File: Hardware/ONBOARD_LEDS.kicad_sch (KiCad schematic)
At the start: 38 parts, among them U10 SN74HC594DR, U9 SN74HC594DR

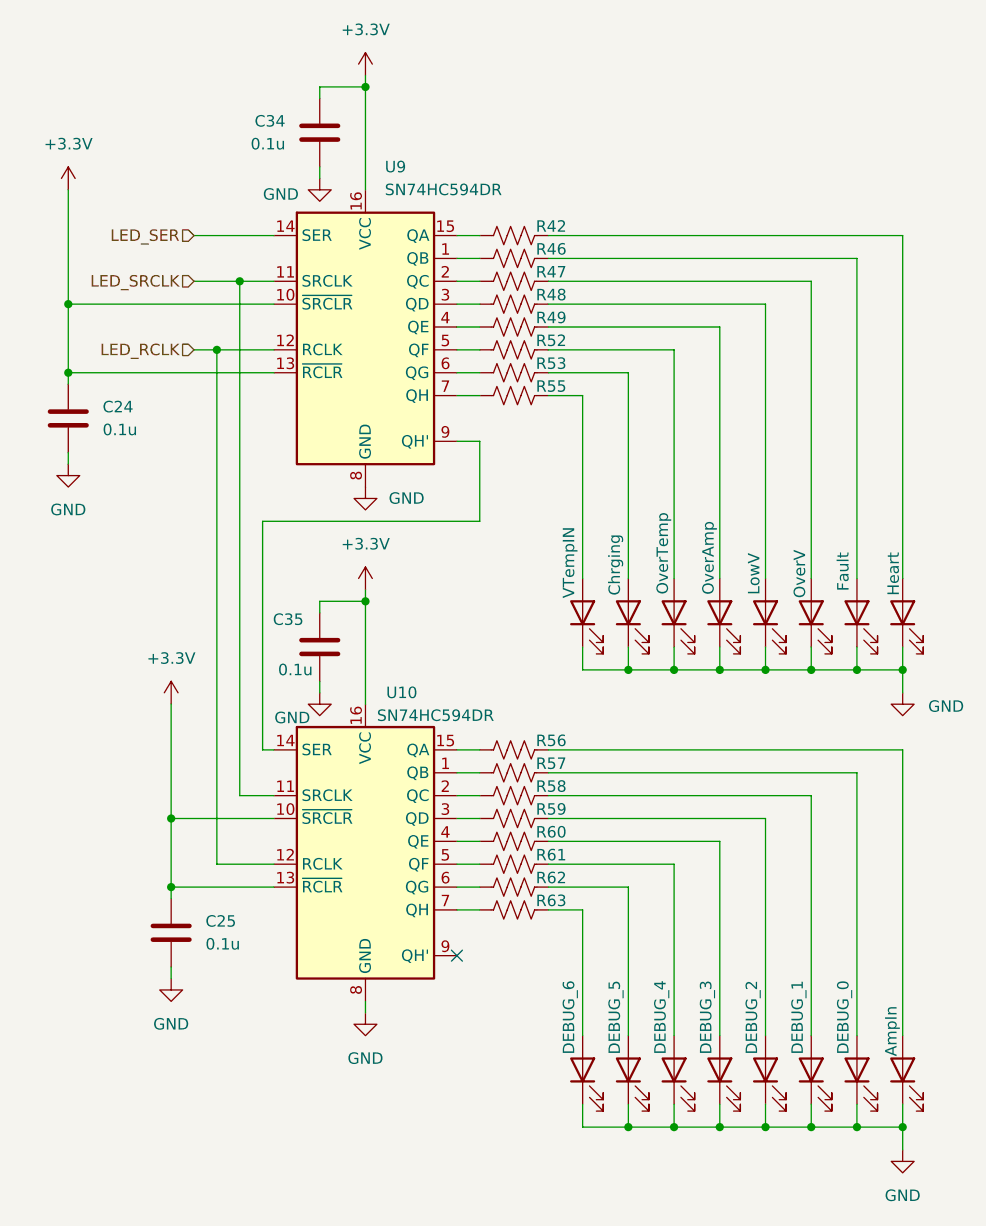
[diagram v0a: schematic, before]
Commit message: Schematic polishes, layout WIP
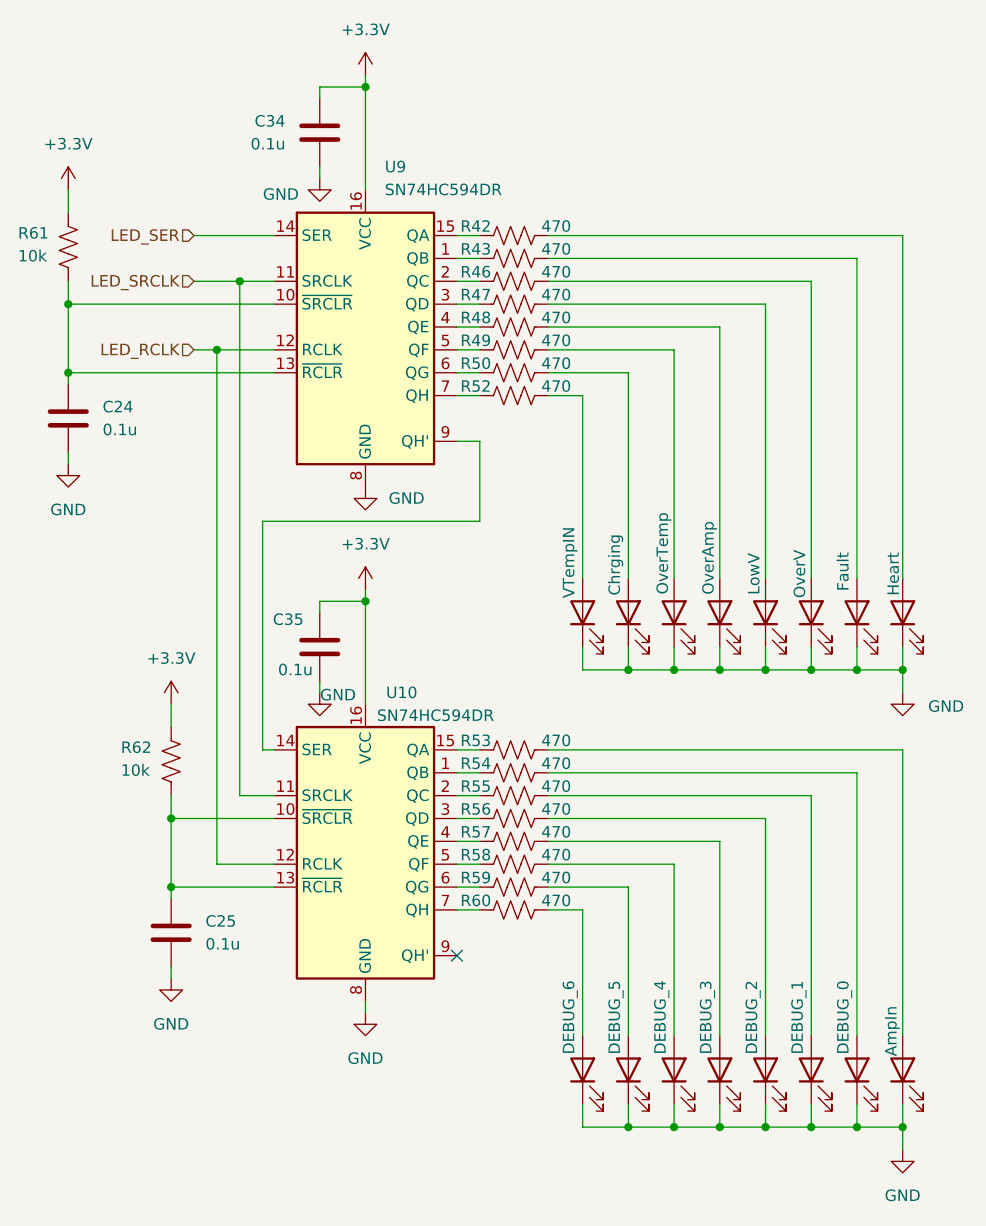
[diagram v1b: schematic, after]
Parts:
- removed R63: 150, Resistor_SMD:R_0603_1608Metric, symbol Device:R_US
- added R43, R50, R54: 470, Resistor_SMD:R_0603_1608Metric, symbol Device:R_US
- C24, C25, C34, C35: footprint Capacitor_SMD:C_0603_1608Metric_Pad1.08x0.95mm_HandSolder -> Capacitor_SMD:C_0603_1608Metric
- R42, R46, R47, R48, R49, R52, R53, R55, R57, R58, R59, R60: value 150 -> 470; P/N CRCW0603150RFKEC -> CRCW1206470RFKEA
- R56: value 120 -> 470; P/N CRCW0603120RFKEC -> CRCW1206470RFKEA
- R61, R62: value 150 -> 10k; Manufactuerer Vishay -> (none); Mouser Part Number (none) -> 71-CRCW060310K0FKEI; P/N CRCW0603150RFKEC -> CRCW060310K0FKEI
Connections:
- net +3.3V: now also R61.1, R62.1; no longer C24.1, C25.1, U10.10 (~{SRCLR}), U10.13 (~{RCLR}), U9.10 (~{SRCLR}), U9.13 (~{RCLR})
- net at OverTemp1.2 (A): now also R49.2; no longer R52.2
- net at U9.6 (QG): now also R50.1; no longer R53.1
- net at Chrging1.2 (A): now also R50.2; no longer R53.2
- net at DEBUG_3.2 (A): now also R57.2; no longer R60.2
- net at R47.1: now also U9.3 (QD); no longer U9.2 (QC)
- net at R47.2: now also LowV1.2 (A); no longer OverV1.2 (A)
- net at R61.2: now also C24.1, U9.10 (~{SRCLR}), U9.13 (~{RCLR}); no longer DEBUG_4.2 (A)
- net at U10.6 (QG): now also R59.1; no longer R62.1
- net at DEBUG_5.2 (A): now also R59.2; no longer R62.2
- net at R48.2: now also OverAmp1.2 (A); no longer LowV1.2 (A)
- net at DEBUG_6.2 (A): now also R60.2
- net at U10.4 (QE): now also R57.1; no longer R60.1
- net at U10.2 (QC): now also R55.1; no longer R58.1
- net at R58.2: now also DEBUG_4.2 (A); no longer DEBUG_1.2 (A)
- net at U9.4 (QE): now also R48.1; no longer R49.1
- net at VTempIN1.2 (A): now also R52.2; no longer R55.2
- net at R56.1: now also U10.3 (QD); no longer U10.15 (QA)
- net at R56.2: now also DEBUG_2.2 (A); no longer AmpIn1.2 (A)
- net at DEBUG_0.2 (A): now also R54.2; no longer R57.2
- net at R46.1: now also U9.2 (QC); no longer U9.1 (QB)
- net at R52.1: now also U9.7 (QH); no longer U9.5 (QF)
- net at R46.2: now also OverV1.2 (A); no longer Fault1.2 (A)
- net at U10.1 (QB): now also R54.1; no longer R57.1
- net at U10.5 (QF): now also R58.1; no longer R61.1
- net at U10.7 (QH): now also R60.1
- new net: R43.1, U9.1 (QB)
- new net: Fault1.2 (A), R43.2
- new net: C25.1, R62.2, U10.10 (~{SRCLR}), U10.13 (~{RCLR})
- new net: R53.1, U10.15 (QA)
- new net: AmpIn1.2 (A), R53.2
- new net: DEBUG_1.2 (A), R55.2
- new net: R49.1, U9.5 (QF)

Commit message: RevB layout completed
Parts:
- D14: renamed from Heart1; value Heart -> DEBUG
- D15: renamed from Fault1; value Fault -> ModuleFault[0]
- D16: renamed from OverV1; value OverV -> ModuleFault[1]
- D17: renamed from LowV1; value LowV -> ModuleFault[2]
- D18: renamed from OverAmp1; value OverAmp -> ModuleFault[3]
- D19: renamed from OverTemp1; value OverTemp -> ModuleFault[4]
- D20: renamed from Chrging1; value Chrging -> WatchdogErr
- D21: renamed from VTempIN1; value VTempIN -> AmpIN
- D22: renamed from AmpIn1; value AmpIn -> VTempIN
- D23: renamed from DEBUG_0; value DEBUG_0 -> Chrging
- D24: renamed from DEBUG_1; value DEBUG_1 -> OverTemp
- D25: renamed from DEBUG_2; value DEBUG_2 -> OverAmp
- D26: renamed from DEBUG_3; value DEBUG_3 -> LowV
- D28: renamed from DEBUG_5; value DEBUG_5 -> Fault
- D29: renamed from DEBUG_6; value DEBUG_6 -> Heart
- D30: renamed from DEBUG_4; value DEBUG_4 -> OverV
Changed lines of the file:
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@@
 		(on_board yes)
 		(dnp no)
-		(property "Reference" "OverTemp1"
+		(property "Reference" "D19"
 			(at 191.77 94.2975 0)
 			(effects
@@
 			)
 		)
-		(property "Value" "OverTemp"
-			(at 182.88 86.106 0)
+		(property "Value" "ModuleFault[4]"
+			(at 182.372 83.312 0)
 			(effects
 				(font
@@
 			(project "BPS-Leader"
 				(path "/fb37da34-e420-4994-8cc1-079e8c0fa48e/ec328d6f-4db5-4eba-b704-0212808a8e56"
-					(reference "OverTemp1")
+					(reference "D19")
 					(unit 1)
 				)
@@
 		(on_board yes)
 		(dnp no)
-		(property "Reference" "DEBUG_3"
+		(property "Reference" "D26"
 			(at 196.85 145.0975 0)
 			(effects
@@
 			)
 		)
-		(property "Value" "DEBUG_3"
+		(property "Value" "LowV"
 			(at 187.706 137.668 0)
 			(effects
@@
 			(project "BPS-Leader"
 				(path "/fb37da34-e420-4994-8cc1-079e8c0fa48e/ec328d6f-4db5-4eba-b704-0212808a8e56"
-					(reference "DEBUG_3")
+					(reference "D26")
 					(unit 1)
 				)
@@
 		(on_board yes)
 		(dnp no)
-		(property "Reference" "DEBUG_4"
+		(property "Reference" "D30"
 			(at 191.77 145.0975 0)
 			(effects
@@
 			)
 		)
-		(property "Value" "DEBUG_4"
+		(property "Value" "OverV"
 			(at 182.626 137.668 0)
 			(effects
@@
 			(project "BPS-Leader"
 				(path "/fb37da34-e420-4994-8cc1-079e8c0fa48e/ec328d6f-4db5-4eba-b704-0212808a8e56"
-					(reference "DEBUG_4")
+					(reference "D30")
 					(unit 1)
 				)
@@
 		(on_board yes)
 		(dnp no)
-		(property "Reference" "Heart1"
+		(property "Reference" "D14"
 			(at 217.17 94.2975 0)
 			(effects
@@
 			)
 		)
-		(property "Value" "Heart"
-			(at 208.534 88.392 0)
+		(property "Value" "DEBUG"
+			(at 208.026 87.122 0)
 			(effects
 				(font
@@
 			(project "BPS-Leader"
 				(path "/fb37da34-e420-4994-8cc1-079e8c0fa48e/ec328d6f-4db5-4eba-b704-0212808a8e56"
-					(reference "Heart1")
+					(reference "D14")
 					(unit 1)
 				)
@@
 		(on_board yes)
 		(dnp no)
-		(property "Reference" "LowV1"
+		(property "Reference" "D17"
 			(at 201.93 94.2975 0)
 			(effects
@@
 			)
 		)
-		(property "Value" "LowV"
-			(at 193.04 88.392 0)
+		(property "Value" "ModuleFault[2]"
+			(at 193.04 83.566 0)
 			(effects
 				(font
@@
 			(project "BPS-Leader"
 				(path "/fb37da34-e420-4994-8cc1-079e8c0fa48e/ec328d6f-4db5-4eba-b704-0212808a8e56"
-					(reference "LowV1")
+					(reference "D17")
 					(unit 1)
 				)
@@
 		(on_board yes)
 		(dnp no)
-		(property "Reference" "DEBUG_6"
+		(property "Reference" "D29"
 			(at 181.61 145.0975 0)
 			(effects
@@
 			)
 		)
-		(property "Value" "DEBUG_6"
+		(property "Value" "Heart"
 			(at 172.466 137.668 0)
 			(effects
@@
 			(project "BPS-Leader"
 				(path "/fb37da34-e420-4994-8cc1-079e8c0fa48e/ec328d6f-4db5-4eba-b704-0212808a8e56"
-					(reference "DEBUG_6")
+					(reference "D29")
 					(unit 1)
 				)
@@
 		(on_board yes)
 		(dnp no)
-		(property "Reference" "Chrging1"
+		(property "Reference" "D20"
 			(at 186.69 94.2975 0)
 			(effects
@@
 			)
 		)
-		(property "Value" "Chrging"
-			(at 177.546 87.376 0)
+		(property "Value" "WatchdogErr"
+			(at 177.292 84.328 0)
 			(effects
 				(font
@@
 			(project "BPS-Leader"
 				(path "/fb37da34-e420-4994-8cc1-079e8c0fa48e/ec328d6f-4db5-4eba-b704-0212808a8e56"
-					(reference "Chrging1")
+					(reference "D20")
 					(unit 1)
 				)
@@
 		(on_board yes)
 		(dnp no)
-		(property "Reference" "DEBUG_5"
+		(property "Reference" "D28"
 			(at 186.69 145.0975 0)
 			(effects
@@
 			)
 		)
-		(property "Value" "DEBUG_5"
+		(property "Value" "Fault"
 			(at 177.546 137.668 0)
 			(effects
@@
 			(project "BPS-Leader"
 				(path "/fb37da34-e420-4994-8cc1-079e8c0fa48e/ec328d6f-4db5-4eba-b704-0212808a8e56"
-					(reference "DEBUG_5")
+					(reference "D28")
 					(unit 1)
 				)
@@
 		(on_board yes)
 		(dnp no)
-		(property "Reference" "VTempIN1"
+		(property "Reference" "D21"
 			(at 181.61 94.2975 0)
 			(effects
@@
 			)
 		)
-		(property "Value" "VTempIN"
+		(property "Value" "AmpIN"
 			(at 172.466 87.122 0)
 			(effects
@@
 			(project "BPS-Leader"
 				(path "/fb37da34-e420-4994-8cc1-079e8c0fa48e/ec328d6f-4db5-4eba-b704-0212808a8e56"
-					(reference "VTempIN1")
+					(reference "D21")
 					(unit 1)
 				)
@@
 		(on_board yes)
 		(dnp no)
-		(property "Reference" "DEBUG_1"
+		(property "Reference" "D24"
 			(at 207.01 145.0975 0)
 			(effects
@@
 			)
 		)
-		(property "Value" "DEBUG_1"
+		(property "Value" "OverTemp"
 			(at 197.866 137.668 0)
 			(effects
@@
 			(project "BPS-Leader"
 				(path "/fb37da34-e420-4994-8cc1-079e8c0fa48e/ec328d6f-4db5-4eba-b704-0212808a8e56"
-					(reference "DEBUG_1")
+					(reference "D24")
 					(unit 1)
 				)
@@
 		(on_board yes)
 		(dnp no)
-		(property "Reference" "DEBUG_0"
+		(property "Reference" "D23"
 			(at 212.09 145.0975 0)
 			(effects
@@
 			)
 		)
-		(property "Value" "DEBUG_0"
+		(property "Value" "Chrging"
 			(at 202.946 137.668 0)
 			(effects
@@
 			(project "BPS-Leader"
 				(path "/fb37da34-e420-4994-8cc1-079e8c0fa48e/ec328d6f-4db5-4eba-b704-0212808a8e56"
-					(reference "DEBUG_0")
+					(reference "D23")
 					(unit 1)
 				)
@@
 		(on_board yes)
 		(dnp no)
-		(property "Reference" "DEBUG_2"
+		(property "Reference" "D25"
 			(at 201.93 145.0975 0)
 			(effects
@@
 			)
 		)
-		(property "Value" "DEBUG_2"
+		(property "Value" "OverAmp"
 			(at 192.786 137.668 0)
 			(effects
@@
 			(project "BPS-Leader"
 				(path "/fb37da34-e420-4994-8cc1-079e8c0fa48e/ec328d6f-4db5-4eba-b704-0212808a8e56"
-					(reference "DEBUG_2")
+					(reference "D25")
 					(unit 1)
 				)
@@
 		(on_board yes)
 		(dnp no)
-		(property "Reference" "OverAmp1"
+		(property "Reference" "D18"
 			(at 196.85 94.2975 0)
 			(effects
@@
 			)
 		)
-		(property "Value" "OverAmp"
-			(at 187.96 86.614 0)
+		(property "Value" "ModuleFault[3]"
+			(at 187.706 83.566 0)
 			(effects
 				(font
@@
 			(project "BPS-Leader"
 				(path "/fb37da34-e420-4994-8cc1-079e8c0fa48e/ec328d6f-4db5-4eba-b704-0212808a8e56"
-					(reference "OverAmp1")
+					(reference "D18")
 					(unit 1)
 				)
@@
 		(on_board yes)
 		(dnp no)
-		(property "Reference" "AmpIn1"
+		(property "Reference" "D22"
 			(at 217.17 145.0975 0)
 			(effects
@@
 			)
 		)
-		(property "Value" "AmpIn"
+		(property "Value" "VTempIN"
 			(at 208.28 139.192 0)
 			(effects
@@
 			(project "BPS-Leader"
 				(path "/fb37da34-e420-4994-8cc1-079e8c0fa48e/ec328d6f-4db5-4eba-b704-0212808a8e56"
-					(reference "AmpIn1")
+					(reference "D22")
 					(unit 1)
 				)
@@
 		(on_board yes)
 		(dnp no)
-		(property "Reference" "Fault1"
+		(property "Reference" "D15"
 			(at 212.09 94.2975 0)
 			(effects
@@
 			)
 		)
-		(property "Value" "Fault"
-			(at 202.946 88.138 0)
+		(property "Value" "ModuleFault[0]"
+			(at 202.692 83.312 0)
 			(effects
 				(font
@@
 			(project "BPS-Leader"
 				(path "/fb37da34-e420-4994-8cc1-079e8c0fa48e/ec328d6f-4db5-4eba-b704-0212808a8e56"
-					(reference "Fault1")
+					(reference "D15")
 					(unit 1)
 				)
@@
 		(on_board yes)
 		(dnp no)
-		(property "Reference" "OverV1"
+		(property "Reference" "D16"
 			(at 207.01 94.2975 0)
 			(effects
@@
 			)
 		)
-		(property "Value" "OverV"
-			(at 198.12 88.392 0)
+		(property "Value" "ModuleFault[1]"
+			(at 197.612 83.566 0)
 			(effects
 				(font
@@
 			(project "BPS-Leader"
 				(path "/fb37da34-e420-4994-8cc1-079e8c0fa48e/ec328d6f-4db5-4eba-b704-0212808a8e56"
-					(reference "OverV1")
+					(reference "D16")
 					(unit 1)
 				)

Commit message: JLC Production Files
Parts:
- C24, C25, C34, C35: LCSC (none) -> C14663
- D14, D20, D21, D22, D23, D24, D25, D26, D28, D29, D30: LCSC (none) -> C84263
- D15, D16, D17, D18, D19: LCSC (none) -> C7371904
- R42, R43, R46, R47, R48, R49, R50, R52, R53, R54, R55, R56, R57, R58, R59, R60: LCSC (none) -> C23179
- R61, R62: LCSC (none) -> C25804
- U10, U9: LCSC (none) -> C91727

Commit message: condensed custom lirbraries
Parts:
- U10, U9: footprint SN74HC594DR:SOIC127P600X175-16N -> CustomKiCad-Library:SOIC127P600X175-16N
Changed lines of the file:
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@@
 			)
 		)
-		(property "Footprint" "SN74HC594DR:SOIC127P600X175-16N"
+		(property "Footprint" "CustomKiCad-Library:SOIC127P600X175-16N"
 			(at 149.86 60.96 0)
 			(effects
@@
 			)
 		)
-		(property "Datasheet" "https://www.ti.com/lit/gpn/sn74hc594"
+		(property "Datasheet" "https://www.ti.com/lit/ds/symlink/sn74hc594.pdf"
 			(at 149.86 60.96 0)
 			(effects
@@
 			)
 		)
-		(property "Footprint" "SN74HC594DR:SOIC127P600X175-16N"
+		(property "Footprint" "CustomKiCad-Library:SOIC127P600X175-16N"
 			(at 149.86 118.11 0)
 			(effects

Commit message: JLCPCB ouput files
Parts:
- R61, R62: P/N CRCW060310K0FKEI -> CRCW060310K0FKEI
